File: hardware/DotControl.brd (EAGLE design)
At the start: 30.7 x 65 mm, 24 parts, among them CN1 1X4-BIG, J3 USB-MICROB, SW2 Previous, SW5 Previous, SW6 Next, SW8 Ok, U1 ATMEGA328P-MU-QFN32, U2 TMP102

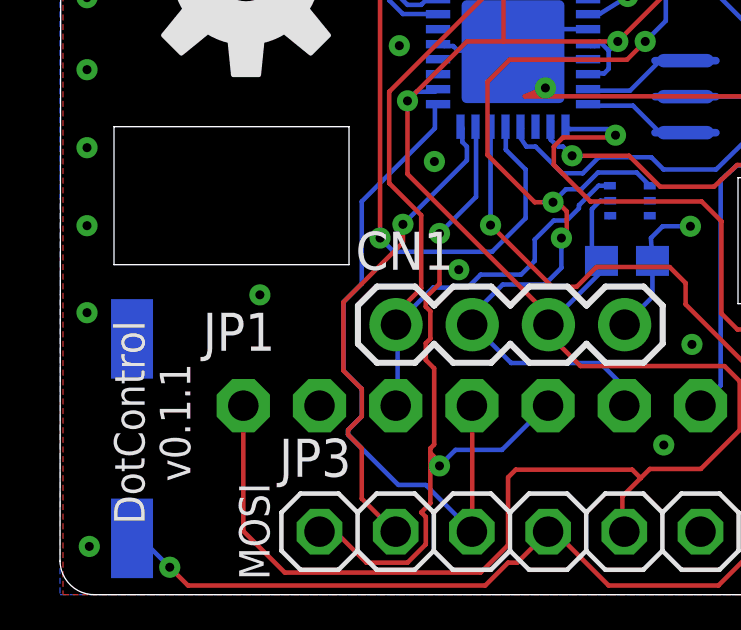
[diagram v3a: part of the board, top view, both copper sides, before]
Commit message: Add CryptoAuthentication module
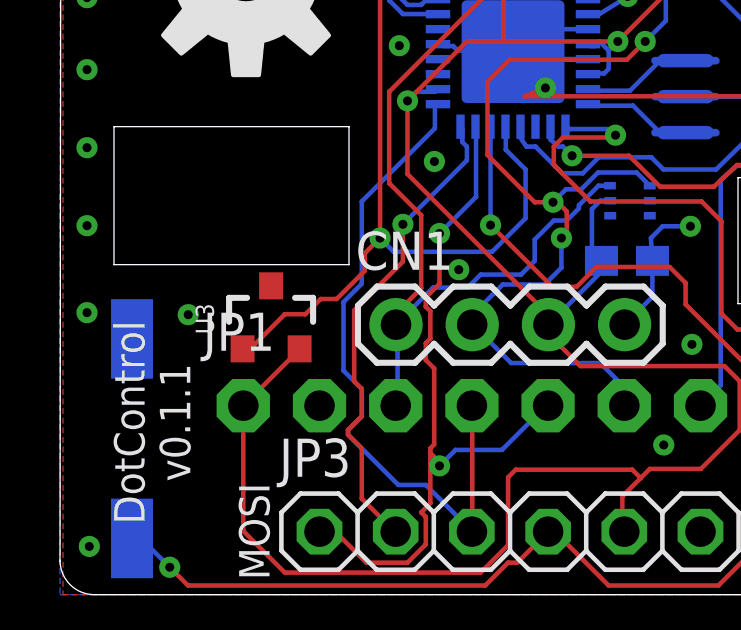
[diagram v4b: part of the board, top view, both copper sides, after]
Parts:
- added U3: ATSHA204-TSU, SparkFun-IC-Special-Function:SOT23-3
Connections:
- net +3V3: now also U3.2
- net ADCENA: now also U3.1
- net GND: now also U3.3
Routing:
- net ADCENA: track 60.8 -> 67.2 mm
- net +3V3: track 151.1 -> 153.8 mm
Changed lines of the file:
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@@
 <element name="U2" library="SparkFun" package="SOT563" value="TMP102" x="18.9992" y="13.1318" rot="MR270"/>
 <element name="C3" library="resistor" package="C0603" value="0.1uF" x="18.8976" y="11.1252" rot="MR180"/>
+<element name="U3" library="SparkFun-IC-Special-Function" package="SOT23-3" value="ATSHA204-TSU" x="7.0358" y="9.1948">
+<attribute name="PROD_ID" value="IC-11208" x="7.0358" y="10.16" size="1.778" layer="27" display="off"/>
+</element>
 </elements>
 <signals>
@@
 <via x="23.5278" y="8.1392" extent="1-16" drill="0.3"/>
 <via x="21.0132" y="12.2794" extent="1-16" drill="0.3"/>
-<via x="6.6622" y="9.9934" extent="1-16" drill="0.3"/>
+<via x="4.2746" y="9.333" extent="1-16" drill="0.3"/>
 <via x="20.1242" y="4.9896" extent="1-16" drill="0.3"/>
 <via x="13.2916" y="10.8316" extent="1-16" drill="0.3"/>
@@
 <via x="12.4788" y="14.4384" extent="1-16" drill="0.3"/>
 <via x="11.3104" y="18.2992" extent="1-16" drill="0.3"/>
+<contactref element="U3" pad="3"/>
 <wire x1="16.256" y1="17.85" x2="16.1798" y2="17.8308" width="0" layer="19" extent="16-16"/>
 </signal>
@@
 <wire x1="13.5636" y1="14.9352" x2="13.4112" y2="15.0876" width="0.1524" layer="16"/>
 <wire x1="13.5636" y1="14.478" x2="13.5636" y2="14.9352" width="0.1524" layer="16"/>
-<wire x1="11.43" y1="11.7348" x2="11.43" y2="12.3444" width="0.1524" layer="1"/>
-<wire x1="9.4488" y1="9.7536" x2="11.43" y2="11.7348" width="0.1524" layer="1"/>
-<wire x1="9.4488" y1="7.4676" x2="9.4488" y2="9.7536" width="0.1524" layer="1"/>
 <wire x1="10.0584" y1="5.9436" x2="10.0584" y2="6.858" width="0.1524" layer="1"/>
 <wire x1="9.6012" y1="5.4864" x2="10.0584" y2="5.9436" width="0.1524" layer="1"/>
@@
 <via x="11.43" y="12.3444" extent="1-16" drill="0.3"/>
 <wire x1="11.43" y1="12.3444" x2="13.5636" y2="14.478" width="0.1524" layer="16"/>
-<wire x1="9.4488" y1="7.4676" x2="10.0584" y2="6.858" width="0.1524" layer="1"/>
+<wire x1="11.43" y1="12.3444" x2="11.43" y2="11.0998" width="0.1524" layer="1"/>
+<wire x1="11.43" y1="11.0998" x2="9.8044" y2="9.4742" width="0.1524" layer="1"/>
+<wire x1="9.8044" y1="9.4742" x2="9.8044" y2="7.112" width="0.1524" layer="1"/>
+<wire x1="9.8044" y1="7.112" x2="10.0584" y2="6.858" width="0.1524" layer="1"/>
 </signal>
 <signal name="SDA">
@@
 <wire x1="17.7292" y1="12.8524" x2="17.7292" y2="11.4436" width="0.1524" layer="16"/>
 <wire x1="17.7292" y1="11.4436" x2="18.0476" y2="11.1252" width="0.1524" layer="16"/>
+<contactref element="U3" pad="2"/>
+<wire x1="7.9858" y1="8.1948" x2="7.9858" y2="8.1758" width="0.1524" layer="1"/>
+<wire x1="7.9858" y1="8.1758" x2="6.11" y2="6.3" width="0.1524" layer="1"/>
 </signal>
 <signal name="PUSH">
@@
 <wire x1="14.859" y1="15.5702" x2="14.859" y2="15.591" width="0.1524" layer="16"/>
 <wire x1="14.859" y1="15.591" x2="14.85" y2="15.6" width="0.1524" layer="16"/>
+<contactref element="U3" pad="1"/>
+<wire x1="6.0858" y1="8.1948" x2="6.3406" y2="8.1948" width="0.1524" layer="1"/>
+<wire x1="6.3406" y1="8.1948" x2="7.493" y2="9.3472" width="0.1524" layer="1"/>
+<wire x1="7.493" y1="9.3472" x2="8.1788" y2="9.3472" width="0.1524" layer="1"/>
+<wire x1="8.1788" y1="9.3472" x2="8.6868" y2="9.8552" width="0.1524" layer="1"/>
+<wire x1="8.6868" y1="9.8552" x2="9.2202" y2="9.8552" width="0.1524" layer="1"/>
+<wire x1="9.2202" y1="9.8552" x2="10.16" y2="10.795" width="0.1524" layer="1"/>
+<wire x1="10.16" y1="10.795" x2="10.16" y2="11.3792" width="0.1524" layer="1"/>
+<wire x1="10.16" y1="11.3792" x2="10.668" y2="11.8872" width="0.1524" layer="1"/>
 </signal>
 <signal name="TXD">

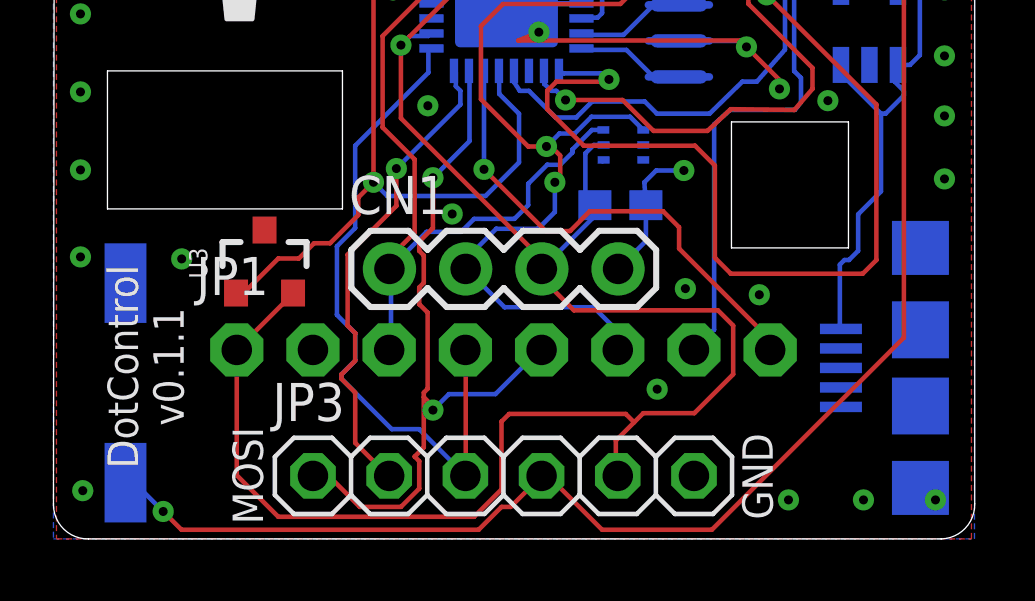
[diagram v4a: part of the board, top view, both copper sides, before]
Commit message: Reposition crypto module
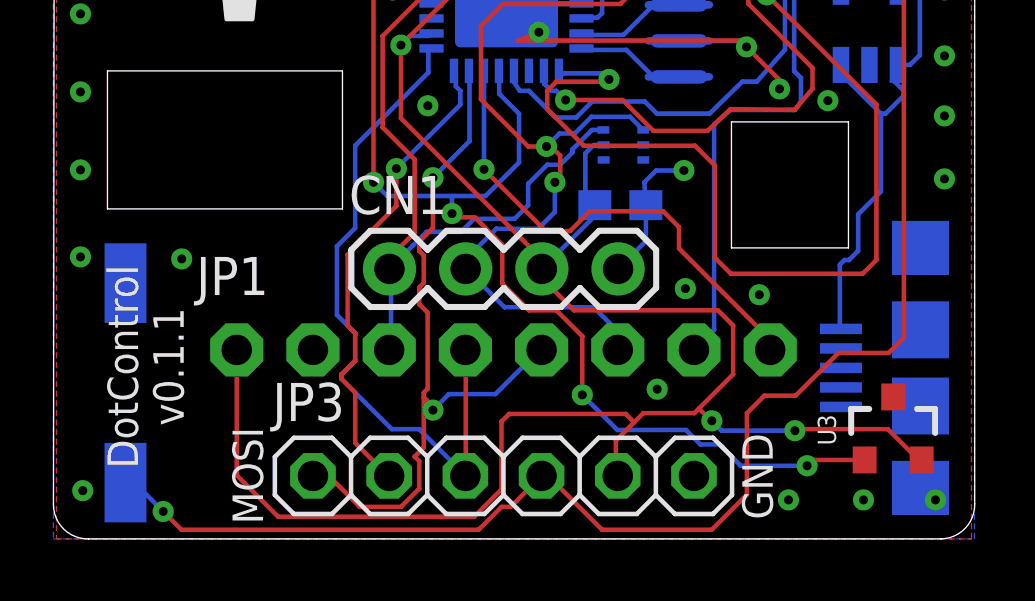
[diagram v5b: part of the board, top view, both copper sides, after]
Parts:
- moved U3 21.7 mm to (28.0, 3.63)
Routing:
- net ADCENA: track 67.2 -> 80.6 mm, vias 3 -> 6
- net +3V3: track 153.8 -> 159.3 mm, vias 5 -> 7
- net RST: track 60.8 -> 62.4 mm
- net GND: vias 104 -> 103
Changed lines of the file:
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@@
 <element name="U2" library="SparkFun" package="SOT563" value="TMP102" x="18.9992" y="13.1318" rot="MR270"/>
 <element name="C3" library="resistor" package="C0603" value="0.1uF" x="18.8976" y="11.1252" rot="MR180"/>
-<element name="U3" library="SparkFun-IC-Special-Function" package="SOT23-3" value="ATSHA204-TSU" x="7.0358" y="9.1948">
-<attribute name="PROD_ID" value="IC-11208" x="7.0358" y="10.16" size="1.778" layer="27" display="off"/>
+<element name="U3" library="SparkFun-IC-Special-Function" package="SOT23-3" value="ATSHA204-TSU" x="27.9908" y="3.6322">
+<attribute name="PROD_ID" value="IC-11208" x="27.9908" y="4.5974" size="1.778" layer="27" display="off"/>
 </element>
 </elements>
@@
 <via x="4.2746" y="9.333" extent="1-16" drill="0.3"/>
 <via x="20.1242" y="4.9896" extent="1-16" drill="0.3"/>
-<via x="13.2916" y="10.8316" extent="1-16" drill="0.3"/>
+<wire x1="13.2916" y1="10.8316" x2="13.2916" y2="10.8316" width="0" layer="19" extent="1-16"/>
 <via x="21.064" y="8.3424" extent="1-16" drill="0.3"/>
 <via x="25.8138" y="14.608" extent="1-16" drill="0.3"/>
@@
 <wire x1="28.3464" y1="20.574" x2="25.7556" y2="23.1648" width="0.1524" layer="1"/>
 <wire x1="28.3464" y1="6.7056" x2="28.3464" y2="20.574" width="0.1524" layer="1"/>
-<wire x1="21.9456" y1="0.3048" x2="28.3464" y2="6.7056" width="0.1524" layer="1"/>
 <wire x1="18.288" y1="0.3048" x2="21.9456" y2="0.3048" width="0.1524" layer="1"/>
 <wire x1="16.6116" y1="1.9812" x2="18.288" y2="0.3048" width="0.1524" layer="1"/>
@@
 <via x="16.9164" y="22.86" extent="1-16" drill="0.3"/>
 <via x="3.6576" y="0.9144" extent="1-16" drill="0.3"/>
+<wire x1="21.9456" y1="0.3048" x2="23.114" y2="1.4732" width="0.1524" layer="1"/>
+<wire x1="23.114" y1="1.4732" x2="23.114" y2="4.191" width="0.1524" layer="1"/>
+<wire x1="23.114" y1="4.191" x2="23.6982" y2="4.7752" width="0.1524" layer="1"/>
+<wire x1="23.6982" y1="4.7752" x2="24.7396" y2="4.7752" width="0.1524" layer="1"/>
+<wire x1="24.7396" y1="4.7752" x2="26.162" y2="6.1976" width="0.1524" layer="1"/>
+<wire x1="26.162" y1="6.1976" x2="27.8384" y2="6.1976" width="0.1524" layer="1"/>
+<wire x1="27.8384" y1="6.1976" x2="28.3464" y2="6.7056" width="0.1524" layer="1"/>
 </signal>
 <signal name="+3V3">
@@
 <wire x1="19.3548" y1="3.8862" x2="19.6596" y2="4.191" width="0.1524" layer="1"/>
 <wire x1="19.6596" y1="4.191" x2="21.3614" y2="4.191" width="0.1524" layer="1"/>
-<wire x1="21.3614" y1="4.191" x2="22.6568" y2="5.4864" width="0.1524" layer="1"/>
+<wire x1="21.3614" y1="4.191" x2="21.5138" y2="4.3434" width="0.1524" layer="1"/>
+<wire x1="21.5138" y1="4.3434" x2="22.6568" y2="5.4864" width="0.1524" layer="1"/>
 <wire x1="22.6568" y1="5.4864" x2="22.6568" y2="7.112" width="0.1524" layer="1"/>
 <wire x1="22.6568" y1="7.112" x2="22.1488" y2="7.62" width="0.1524" layer="1"/>
@@
 <wire x1="17.7292" y1="11.4436" x2="18.0476" y2="11.1252" width="0.1524" layer="16"/>
 <contactref element="U3" pad="2"/>
-<wire x1="7.9858" y1="8.1948" x2="7.9858" y2="8.1758" width="0.1524" layer="1"/>
-<wire x1="7.9858" y1="8.1758" x2="6.11" y2="6.3" width="0.1524" layer="1"/>
+<wire x1="28.9408" y1="2.6322" x2="28.8384" y2="2.6322" width="0.1524" layer="1"/>
+<wire x1="28.8384" y1="2.6322" x2="27.813" y2="3.6576" width="0.1524" layer="1"/>
+<wire x1="27.813" y1="3.6576" x2="24.765" y2="3.6576" width="0.1524" layer="1"/>
+<wire x1="24.765" y1="3.6576" x2="24.7142" y2="3.6068" width="0.1524" layer="1"/>
+<via x="24.7142" y="3.6068" extent="1-16" drill="0.3"/>
+<wire x1="24.7142" y1="3.6068" x2="22.2758" y2="3.6068" width="0.1524" layer="16"/>
+<wire x1="22.2758" y1="3.6068" x2="21.9456" y2="3.937" width="0.1524" layer="16"/>
+<via x="21.9456" y="3.937" extent="1-16" drill="0.3"/>
+<wire x1="21.9456" y1="3.937" x2="21.9202" y2="3.937" width="0.1524" layer="1"/>
+<wire x1="21.9202" y1="3.937" x2="21.5138" y2="4.3434" width="0.1524" layer="1"/>
 </signal>
 <signal name="PUSH">
@@
 <contactref element="U1" pad="13"/>
 <contactref element="SW2" pad="2"/>
-<wire x1="11.1252" y1="11.43" x2="14.4018" y2="11.43" width="0.1524" layer="16"/>
+<wire x1="11.1252" y1="11.43" x2="13.2842" y2="11.43" width="0.1524" layer="16"/>
+<wire x1="13.2842" y1="11.43" x2="14.4018" y2="11.43" width="0.1524" layer="16"/>
 <wire x1="10.668" y1="11.8872" x2="11.1252" y2="11.43" width="0.1524" layer="16"/>
 <wire x1="10.668" y1="23.4696" x2="10.668" y2="11.8872" width="0.1524" layer="1"/>
@@
 <wire x1="14.859" y1="15.591" x2="14.85" y2="15.6" width="0.1524" layer="16"/>
 <contactref element="U3" pad="1"/>
-<wire x1="6.0858" y1="8.1948" x2="6.3406" y2="8.1948" width="0.1524" layer="1"/>
-<wire x1="6.3406" y1="8.1948" x2="7.493" y2="9.3472" width="0.1524" layer="1"/>
-<wire x1="7.493" y1="9.3472" x2="8.1788" y2="9.3472" width="0.1524" layer="1"/>
-<wire x1="8.1788" y1="9.3472" x2="8.6868" y2="9.8552" width="0.1524" layer="1"/>
-<wire x1="8.6868" y1="9.8552" x2="9.2202" y2="9.8552" width="0.1524" layer="1"/>
-<wire x1="9.2202" y1="9.8552" x2="10.16" y2="10.795" width="0.1524" layer="1"/>
-<wire x1="10.16" y1="10.795" x2="10.16" y2="11.3792" width="0.1524" layer="1"/>
-<wire x1="10.16" y1="11.3792" x2="10.668" y2="11.8872" width="0.1524" layer="1"/>
+<wire x1="27.0408" y1="2.6322" x2="25.3144" y2="2.6322" width="0.1524" layer="1"/>
+<wire x1="25.3144" y1="2.6322" x2="25.1206" y2="2.4384" width="0.1524" layer="1"/>
+<via x="25.1206" y="2.4384" extent="1-16" drill="0.3"/>
+<wire x1="25.1206" y1="2.4384" x2="22.9108" y2="2.4384" width="0.1524" layer="16"/>
+<wire x1="22.9108" y1="2.4384" x2="22.3012" y2="3.048" width="0.1524" layer="16"/>
+<wire x1="22.3012" y1="3.048" x2="22.3012" y2="3.0734" width="0.1524" layer="16"/>
+<wire x1="22.3012" y1="3.0734" x2="22.2758" y2="3.0988" width="0.1524" layer="16"/>
+<wire x1="22.2758" y1="3.0988" x2="22.2504" y2="3.0988" width="0.1524" layer="16"/>
+<wire x1="22.2504" y1="3.0988" x2="22.1996" y2="3.1496" width="0.1524" layer="16"/>
+<wire x1="22.1996" y1="3.1496" x2="21.5646" y2="3.1496" width="0.1524" layer="16"/>
+<wire x1="21.5646" y1="3.1496" x2="21.082" y2="3.6322" width="0.1524" layer="16"/>
+<wire x1="21.082" y1="3.6322" x2="18.796" y2="3.6322" width="0.1524" layer="16"/>
+<wire x1="18.796" y1="3.6322" x2="17.6276" y2="4.8006" width="0.1524" layer="16"/>
+<via x="17.6276" y="4.8006" extent="1-16" drill="0.3"/>
+<wire x1="17.6276" y1="4.8006" x2="17.6276" y2="6.7564" width="0.1524" layer="1"/>
+<wire x1="17.6276" y1="6.7564" x2="16.764" y2="7.62" width="0.1524" layer="1"/>
+<wire x1="16.764" y1="7.62" x2="15.8496" y2="7.62" width="0.1524" layer="1"/>
+<wire x1="15.8496" y1="7.62" x2="14.9606" y2="8.509" width="0.1524" layer="1"/>
+<wire x1="14.9606" y1="8.509" x2="14.9606" y2="9.8044" width="0.1524" layer="1"/>
+<wire x1="14.9606" y1="9.8044" x2="14.0462" y2="10.7188" width="0.1524" layer="1"/>
+<wire x1="14.0462" y1="10.7188" x2="13.4112" y2="10.7188" width="0.1524" layer="1"/>
+<wire x1="13.4112" y1="10.7188" x2="13.2842" y2="10.8458" width="0.1524" layer="1"/>
+<via x="13.2842" y="10.8458" extent="1-16" drill="0.3"/>
+<wire x1="13.2842" y1="10.8458" x2="13.2842" y2="11.43" width="0.1524" layer="16"/>
 </signal>
 <signal name="TXD">

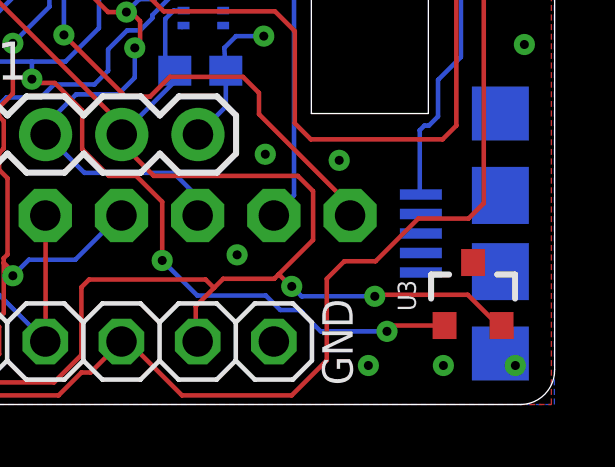
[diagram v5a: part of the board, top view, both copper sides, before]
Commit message: Reposition crypto module
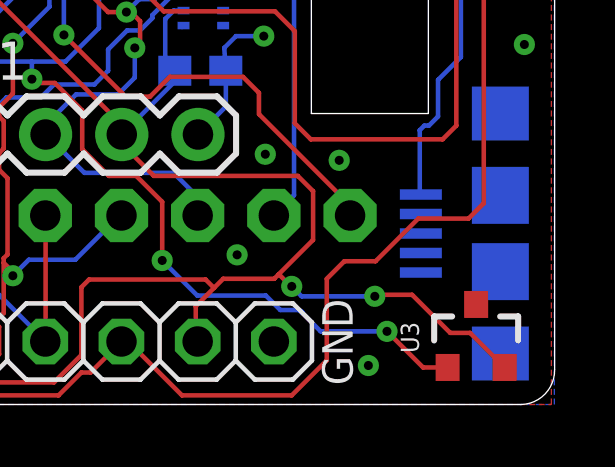
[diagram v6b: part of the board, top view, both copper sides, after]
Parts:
- moved U3 1.40 mm to (28.1, 2.24)
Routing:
- net ADCENA: track 80.6 -> 81.4 mm
- net +3V3: track 159.3 -> 159.9 mm
- net GND: vias 103 -> 101
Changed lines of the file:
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@@
 <element name="U2" library="SparkFun" package="SOT563" value="TMP102" x="18.9992" y="13.1318" rot="MR270"/>
 <element name="C3" library="resistor" package="C0603" value="0.1uF" x="18.8976" y="11.1252" rot="MR180"/>
-<element name="U3" library="SparkFun-IC-Special-Function" package="SOT23-3" value="ATSHA204-TSU" x="27.9908" y="3.6322">
-<attribute name="PROD_ID" value="IC-11208" x="27.9908" y="4.5974" size="1.778" layer="27" display="off"/>
+<element name="U3" library="SparkFun-IC-Special-Function" package="SOT23-3" value="ATSHA204-TSU" x="28.0924" y="2.2352">
+<attribute name="PROD_ID" value="IC-11208" x="28.0924" y="3.2004" size="1.778" layer="27" display="off"/>
 </element>
 </elements>
@@
 <via x="0.9" y="12.3" extent="1-16" drill="0.3"/>
 <via x="0.9" y="9.4" extent="1-16" drill="0.3"/>
-<via x="29.4" y="1.3" extent="1-16" drill="0.3"/>
 <via x="24.5" y="1.3" extent="1-16" drill="0.3"/>
-<via x="27" y="1.3" extent="1-16" drill="0.3"/>
 <via x="0.9762" y="1.608" extent="1-16" drill="0.3"/>
 <polygon width="0.4064" layer="1">
@@
 <via x="4.2746" y="9.333" extent="1-16" drill="0.3"/>
 <via x="20.1242" y="4.9896" extent="1-16" drill="0.3"/>
-<wire x1="13.2916" y1="10.8316" x2="13.2916" y2="10.8316" width="0" layer="19" extent="1-16"/>
 <via x="21.064" y="8.3424" extent="1-16" drill="0.3"/>
 <via x="25.8138" y="14.608" extent="1-16" drill="0.3"/>
@@
 <wire x1="17.7292" y1="11.4436" x2="18.0476" y2="11.1252" width="0.1524" layer="16"/>
 <contactref element="U3" pad="2"/>
-<wire x1="28.9408" y1="2.6322" x2="28.8384" y2="2.6322" width="0.1524" layer="1"/>
-<wire x1="28.8384" y1="2.6322" x2="27.813" y2="3.6576" width="0.1524" layer="1"/>
-<wire x1="27.813" y1="3.6576" x2="24.765" y2="3.6576" width="0.1524" layer="1"/>
 <wire x1="24.765" y1="3.6576" x2="24.7142" y2="3.6068" width="0.1524" layer="1"/>
 <via x="24.7142" y="3.6068" extent="1-16" drill="0.3"/>
@@
 <wire x1="21.9456" y1="3.937" x2="21.9202" y2="3.937" width="0.1524" layer="1"/>
 <wire x1="21.9202" y1="3.937" x2="21.5138" y2="4.3434" width="0.1524" layer="1"/>
+<wire x1="24.765" y1="3.6576" x2="25.9588" y2="3.6576" width="0.1524" layer="1"/>
+<wire x1="25.9588" y1="3.6576" x2="27.2288" y2="2.3876" width="0.1524" layer="1"/>
+<wire x1="27.2288" y1="2.3876" x2="27.89" y2="2.3876" width="0.1524" layer="1"/>
+<wire x1="27.89" y1="2.3876" x2="29.0424" y2="1.2352" width="0.1524" layer="1"/>
 </signal>
 <signal name="PUSH">
@@
 <wire x1="14.859" y1="15.591" x2="14.85" y2="15.6" width="0.1524" layer="16"/>
 <contactref element="U3" pad="1"/>
-<wire x1="27.0408" y1="2.6322" x2="25.3144" y2="2.6322" width="0.1524" layer="1"/>
 <wire x1="25.3144" y1="2.6322" x2="25.1206" y2="2.4384" width="0.1524" layer="1"/>
 <via x="25.1206" y="2.4384" extent="1-16" drill="0.3"/>
@@
 <via x="13.2842" y="10.8458" extent="1-16" drill="0.3"/>
 <wire x1="13.2842" y1="10.8458" x2="13.2842" y2="11.43" width="0.1524" layer="16"/>
+<wire x1="27.1424" y1="1.2352" x2="26.3238" y2="1.2352" width="0.1524" layer="1"/>
+<wire x1="26.3238" y1="1.2352" x2="25.1206" y2="2.4384" width="0.1524" layer="1"/>
 </signal>
 <signal name="TXD">
